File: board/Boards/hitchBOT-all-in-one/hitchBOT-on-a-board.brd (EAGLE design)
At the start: 100 x 55 mm, 16 parts

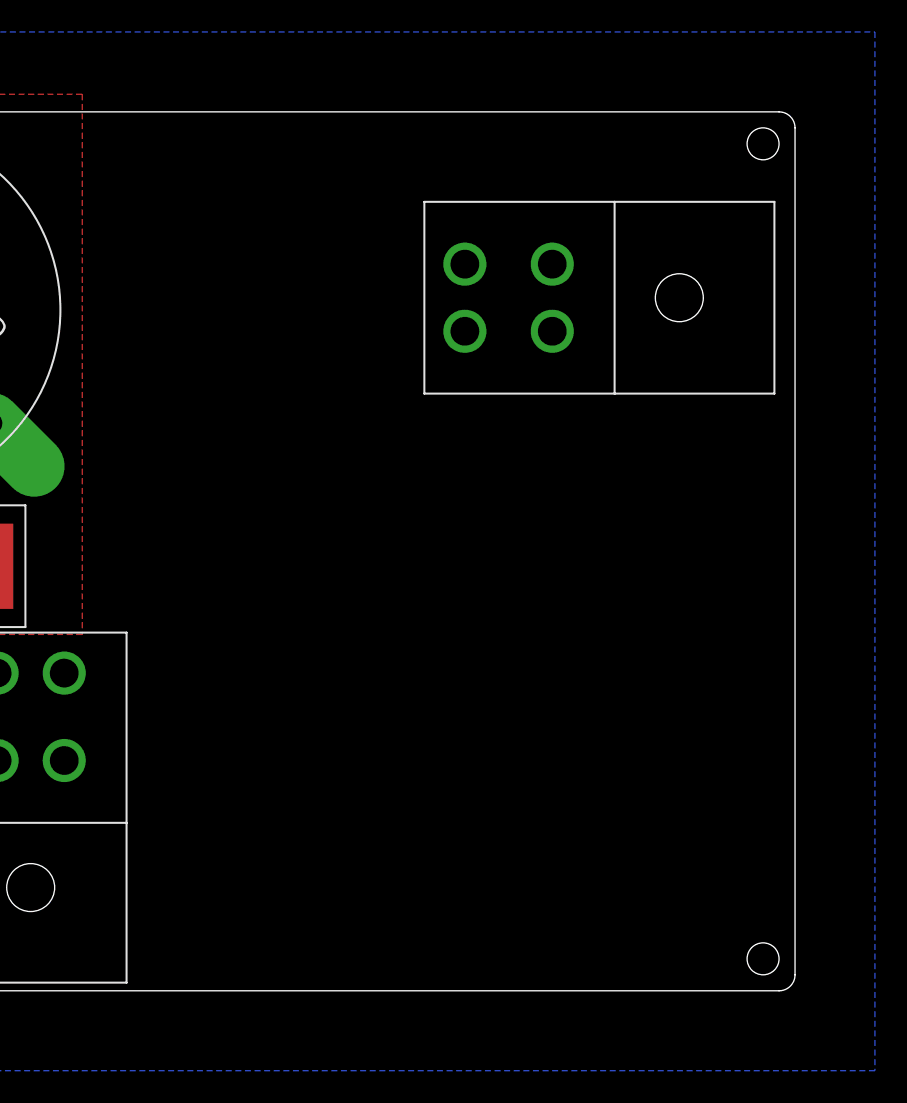
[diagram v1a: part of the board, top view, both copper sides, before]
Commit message: added microcontroller + started 5v switching circuit
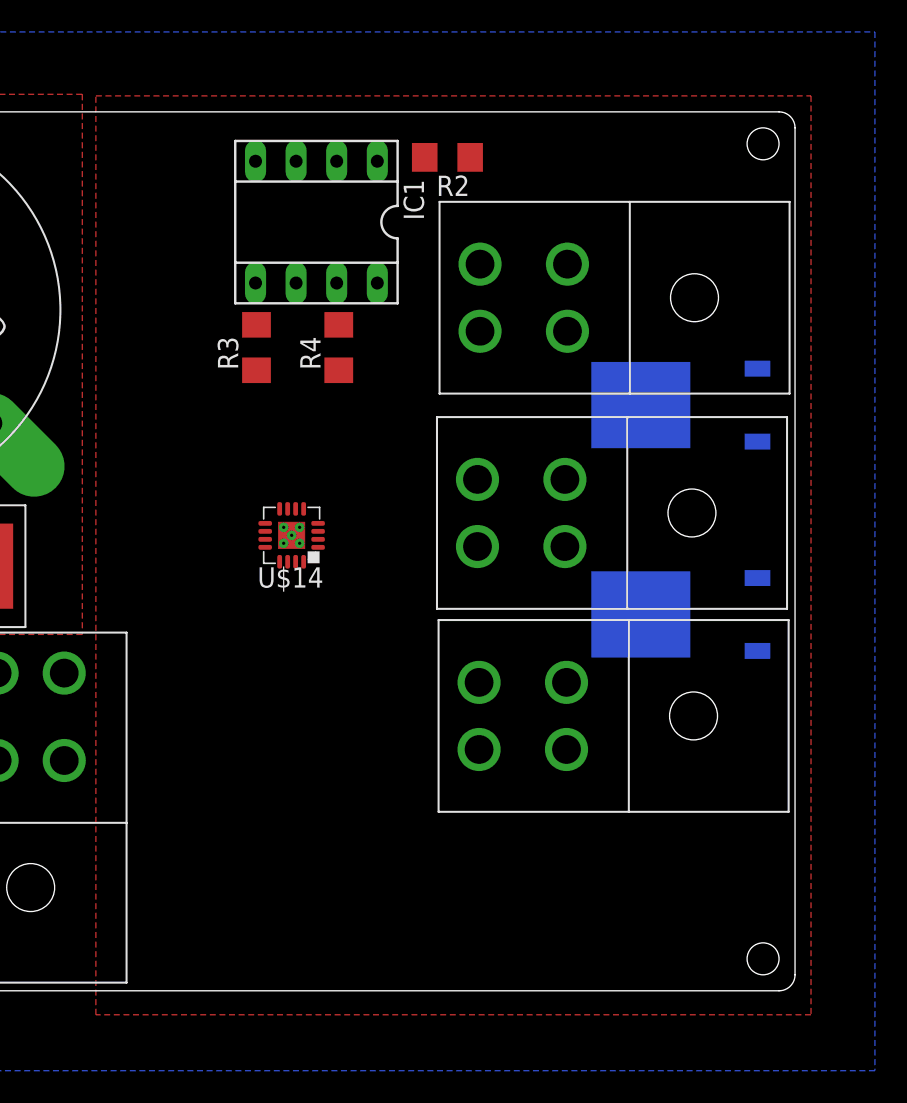
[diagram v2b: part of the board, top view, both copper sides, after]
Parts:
- added IC1: (no value), ic-package:SOCKET-08
- added Q1, Q2: SPD30P06PTO252, transistor-fet:TO252
- added R2, R3, R4: (no value), resistor:R1206
- added U$12, U$13: 2X2-MOLEX, Molex:2X2MOLEX
- added U$14: TPS62133, macgrid:QFN16
- moved U$11 0.95 mm to (83.7, 43.4)
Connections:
- new net N$10: Q2.3, U$12.GNDL, U$12.GNDR
- new net N$11: IC1.7, Q2.1, R4.2
- new net N$12: U$14.10, U$14.11, U$14.12, U$14.13
- new net N$13: IC1.5, Q1.1, R3.2
- new net N$7: IC1.1, R2.2
- new net N$8: R2.1, U$11.POWERL, U$11.POWERR, U$12.POWERL, U$12.POWERR, U$13.POWERL, U$13.POWERR
- new net N$9: Q1.3, U$13.GNDL, U$13.GNDR
- net GND: now also IC1.4, Q1.2, Q2.2, U$14.15, U$14.16, U$14.5, U$14.6, U$14.7, U$14.8, U$14.P$1
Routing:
- added copper zone on layer 1, net N$8
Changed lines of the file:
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@@
 <setting verticaltext="up"/>
 </settings>
-<grid distance="0.1" unitdist="mm" unit="mm" style="lines" multiple="1" display="no" altdistance="0.5" altunitdist="mm" altunit="mm"/>
+<grid distance="0.25" unitdist="mm" unit="mm" style="lines" multiple="1" display="no" altdistance="0.5" altunitdist="mm" altunit="mm"/>
 <layers>
 <layer number="1" name="Top" color="4" fill="1" visible="yes" active="yes"/>
@@
 <element name="U$9" library="macgrid" package="DO-214AB" value="DO-214AB" x="36.14" y="26.63"/>
 <element name="U$10" library="Molex" package="2X2MOLEX" value="2X2-MOLEX" x="16.51" y="34.96" rot="R270"/>
-<element name="U$11" library="Molex" package="2X2MOLEX" value="2X2-MOLEX" x="82.71" y="43.37" rot="R90"/>
+<element name="U$11" library="Molex" package="2X2MOLEX" value="2X2-MOLEX" x="83.66" y="43.37" rot="R90"/>
+<element name="Q1" library="transistor-fet" package="TO252" value="SPD30P06PTO252" x="92.85" y="23.55" smashed="yes" rot="MR270">
+<attribute name="NAME" x="95.39" y="27.36" size="1.27" layer="26" rot="MR0"/>
+</element>
+<element name="Q2" library="transistor-fet" package="TO252" value="SPD30P06PTO252" x="92.85" y="36.65" smashed="yes" rot="MR270">
+<attribute name="NAME" x="95.39" y="40.46" size="1.27" layer="26" rot="MR0"/>
+</element>
+<element name="IC1" library="ic-package" package="SOCKET-08" value="" x="70.05" y="48.1" rot="R180"/>
+<element name="R2" library="resistor" package="R1206" value="" x="78.25" y="52.15" rot="R180"/>
+<element name="R3" library="resistor" package="R1206" value="" x="66.3" y="40.25" rot="R90"/>
+<element name="R4" library="resistor" package="R1206" value="" x="71.45" y="40.25" rot="R90"/>
+<element name="U$12" library="Molex" package="2X2MOLEX" value="2X2-MOLEX" x="83.5" y="29.9" rot="R90"/>
+<element name="U$13" library="Molex" package="2X2MOLEX" value="2X2-MOLEX" x="83.6" y="17.2" rot="R90"/>
+<element name="U$14" library="macgrid" package="QFN16" value="TPS62133" x="68.5" y="28.5" rot="R180"/>
 </elements>
 <signals>
@@
 <contactref element="U$11" pad="GNDL"/>
 <contactref element="U$11" pad="GNDR"/>
-<wire x1="14.41" y1="37.06" x2="23.9" y2="43.79" width="0" layer="19" extent="1-1"/>
+<contactref element="IC1" pad="4"/>
+<contactref element="Q1" pad="2"/>
+<contactref element="Q2" pad="2"/>
+<contactref element="U$14" pad="5"/>
+<contactref element="U$14" pad="6"/>
+<contactref element="U$14" pad="16"/>
+<contactref element="U$14" pad="P$1"/>
+<contactref element="U$14" pad="15"/>
+<contactref element="U$14" pad="7"/>
+<contactref element="U$14" pad="8"/>
+<via x="68.5" y="28.5" extent="1-16" drill="0.2" diameter="0.254"/>
+<via x="68" y="29" extent="1-16" drill="0.2" diameter="0.254"/>
+<via x="69" y="29" extent="1-16" drill="0.2" diameter="0.254"/>
+<via x="68" y="28" extent="1-16" drill="0.2" diameter="0.254"/>
+<via x="69" y="28" extent="1-16" drill="0.2" diameter="0.254"/>
+<wire x1="68.75" y1="30.155" x2="69.25" y2="30.155" width="0" layer="19" extent="1-1"/>
+<wire x1="68.25" y1="30.155" x2="68.75" y2="30.155" width="0" layer="19" extent="1-1"/>
+<wire x1="67.75" y1="30.155" x2="68.25" y2="30.155" width="0" layer="19" extent="1-1"/>
+<wire x1="69" y1="29" x2="69.25" y2="30.155" width="0" layer="19" extent="1-1"/>
+<wire x1="69.25" y1="26.845" x2="69" y2="28" width="0" layer="19" extent="1-1"/>
+<wire x1="68.75" y1="26.845" x2="69.25" y2="26.845" width="0" layer="19" extent="1-1"/>
 <wire x1="10.43" y1="43.79" x2="14.41" y2="37.06" width="0" layer="19" extent="1-1"/>
 <wire x1="15.68" y1="14.73" x2="24.67" y2="14.41" width="0" layer="19" extent="1-1"/>
@@
 <wire x1="6.81" y1="19.47" x2="15.64" y2="19.47" width="0" layer="19" extent="1-1"/>
 <wire x1="6.87" y1="14.73" x2="6.81" y2="19.47" width="0" layer="19" extent="1-1"/>
+<wire x1="23.9" y1="43.79" x2="14.41" y2="37.06" width="0" layer="19" extent="1-1"/>
 </signal>
 <signal name="N$2">
@@
 </polygon>
 </signal>
+<signal name="N$7">
+<contactref element="R2" pad="2"/>
+<contactref element="IC1" pad="1"/>
+<wire x1="73.86" y1="51.91" x2="76.828" y2="52.15" width="0" layer="19" extent="1-1"/>
+</signal>
+<signal name="N$8">
+<contactref element="U$11" pad="POWERL"/>
+<contactref element="U$11" pad="POWERR"/>
+<contactref element="R2" pad="1"/>
+<contactref element="U$12" pad="POWERL"/>
+<contactref element="U$12" pad="POWERR"/>
+<contactref element="U$13" pad="POWERL"/>
+<contactref element="U$13" pad="POWERR"/>
+<polygon width="0.4064" layer="1">
+<vertex x="56.25" y="56"/>
+<vertex x="101" y="56"/>
+<vertex x="101" y="-1.5"/>
+<vertex x="56.25" y="-1.5"/>
+</polygon>
+</signal>
+<signal name="N$9">
+<contactref element="Q1" pad="3"/>
+<contactref element="U$13" pad="GNDL"/>
+<contactref element="U$13" pad="GNDR"/>
+<wire x1="85.7" y1="19.3" x2="90.35" y2="23.55" width="0" layer="19" extent="16-16"/>
+<wire x1="85.7" y1="15.1" x2="85.7" y2="19.3" width="0" layer="19" extent="1-1"/>
+</signal>
+<signal name="N$10">
+<contactref element="Q2" pad="3"/>
+<contactref element="U$12" pad="GNDL"/>
+<contactref element="U$12" pad="GNDR"/>
+<wire x1="85.6" y1="32" x2="90.35" y2="36.65" width="0" layer="19" extent="16-16"/>
+<wire x1="85.6" y1="27.8" x2="85.6" y2="32" width="0" layer="19" extent="1-1"/>
+</signal>
+<signal name="N$11">
+<contactref element="Q2" pad="1"/>
+<contactref element="R4" pad="2"/>
+<contactref element="IC1" pad="7"/>
+<wire x1="71.45" y1="41.672" x2="97.65" y2="38.93" width="0" layer="19" extent="1-16"/>
+<wire x1="71.32" y1="44.29" x2="71.45" y2="41.672" width="0" layer="19" extent="1-1"/>
+</signal>
+<signal name="N$13">
+<contactref element="IC1" pad="5"/>
+<contactref element="Q1" pad="1"/>
+<contactref element="R3" pad="2"/>
+<wire x1="66.3" y1="41.672" x2="97.65" y2="25.83" width="0" layer="19" extent="1-16"/>
+<wire x1="66.24" y1="44.29" x2="66.3" y2="41.672" width="0" layer="19" extent="1-1"/>
+</signal>
+<signal name="N$12">
+<contactref element="U$14" pad="12"/>
+<contactref element="U$14" pad="11"/>
+<contactref element="U$14" pad="10"/>
+<contactref element="U$14" pad="13"/>
+<wire x1="66.845" y1="28.75" x2="66.845" y2="28.25" width="0" layer="19" extent="1-1"/>
+<wire x1="66.845" y1="27.75" x2="66.845" y2="28.25" width="0" layer="19" extent="1-1"/>
+<wire x1="67.75" y1="26.845" x2="66.845" y2="27.75" width="0" layer="19" extent="1-1"/>
+</signal>
 </signals>

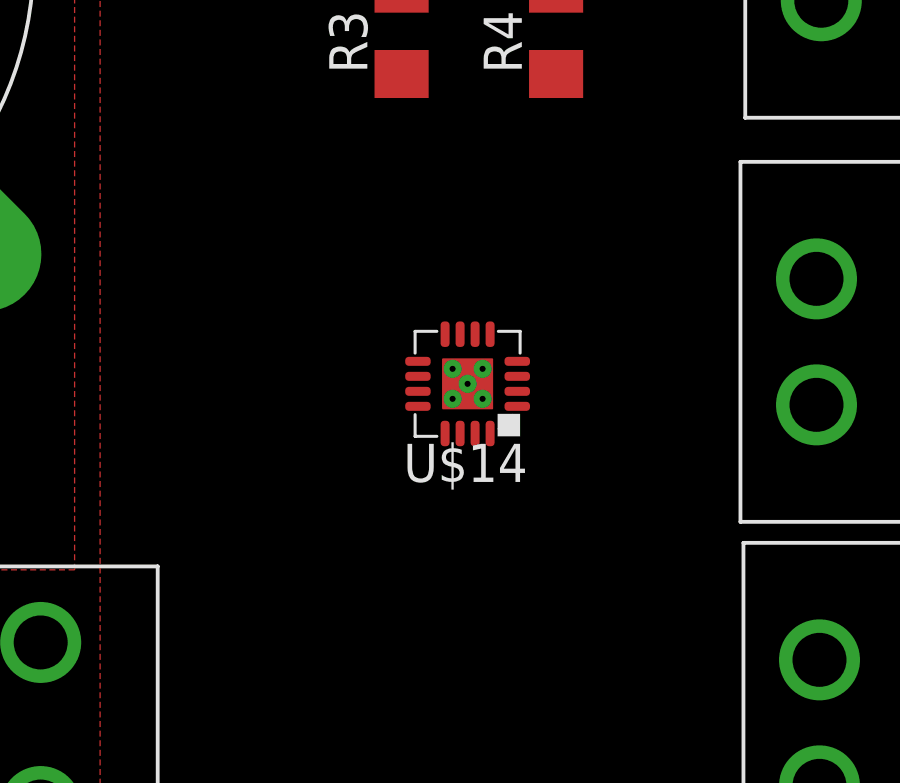
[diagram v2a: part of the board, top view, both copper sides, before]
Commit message: finished initial rough copy of the board, need to add LEDs and writing
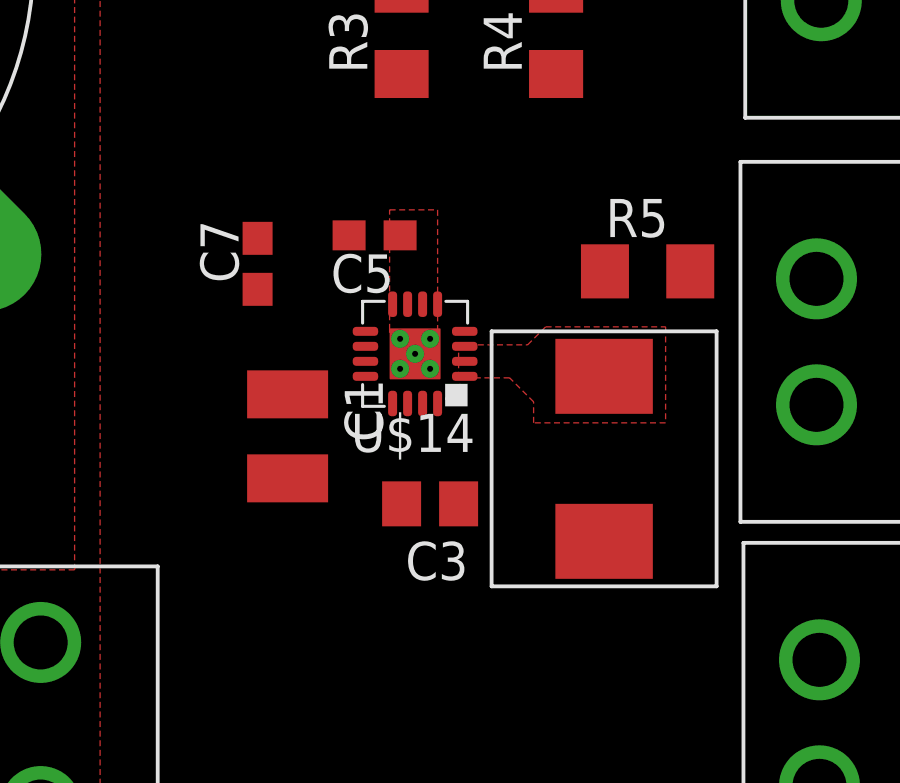
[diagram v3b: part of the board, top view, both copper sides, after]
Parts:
- added C11, C13: SMD-CAP-NICHICON-8MM, macgrid:SMD-CAP-8MM
- added C5: 3300pF, rcl:C0603
- added C7: 0.1uF, rcl:C0603
- added R5: 100k, resistor:R1206
- added U$15: DR73-2R2-R, macgrid:DR73-2R2-R
- C1: value SMD-CAP-NICHICON-8MM -> 10uF; device macgrid:SMD-CAP-8MM -> eagle-ltspice:C1210
- C3: value SMD-CAP-NICHICON-8MM -> 22uF; device macgrid:SMD-CAP-8MM -> rcl:C0805
- moved C1 55.8 mm to (62.5, 26.8), turned to 270 degrees
- moved C3 51.6 mm to (67.2, 24.5), turned to 180 degrees
- moved U$14 2.02 mm to (66.8, 29.5)
- renumbered C2 to C12, C4 to C14
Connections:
- removed net N$12: U$14.10, U$14.11, U$14.12, U$14.13
- new net N$14: U$14.1, U$14.2, U$14.3, U$15.P$1
- new net N$15: C3.1, IC1.8, R2.1, R3.1, R4.1, R5.1, U$14.14, U$15.P$2
- new net N$16: R5.2, U$14.4
- new net N$17: C5.2, U$14.9
- net GND: now also C1.2, C11.P-, C13.P-, C3.2, C5.1, C7.2; no longer C1.P-, C3.P-
- net N$1: now also C11.P+, C13.P+; no longer C1.P+, C3.P+
- net N$8: now also C1.1, C7.1, U$14.10, U$14.11, U$14.12, U$14.13; no longer R2.1
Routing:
- added copper zone on layer 1, net GND
- added copper zone on layer 1, net N$14

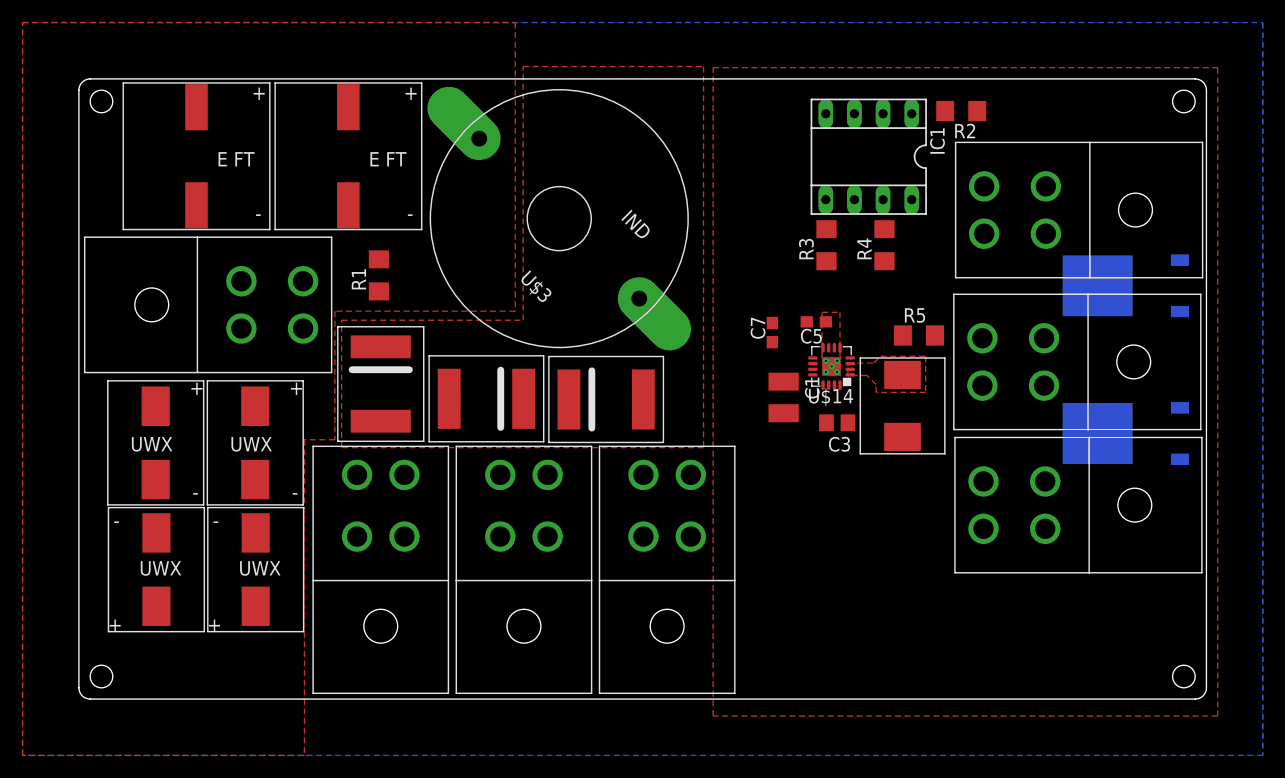
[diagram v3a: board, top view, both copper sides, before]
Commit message: added status LED and molex power adapters for all three voltage areas
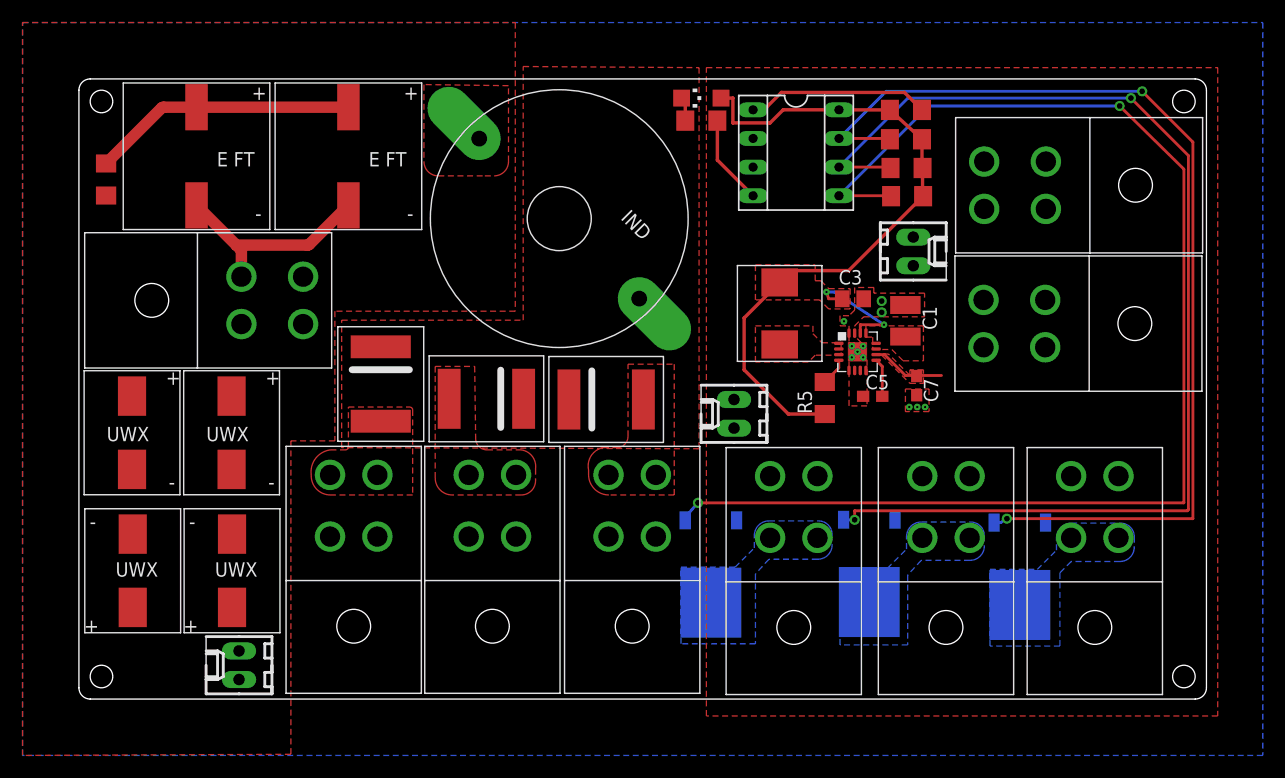
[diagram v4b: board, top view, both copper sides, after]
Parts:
- added J1, J2, J3: 22-27-2021-02, con-molex:6410-02
- added LED1: (no value), led:CHIPLED_1206
- added Q3: SPD30P06PTO252, transistor-fet:TO252
- added R6: (no value), resistor:R1206
- added R7: (no value), rcl:R1206
- added U$16, U$17: 2X2-MOLEX, Molex:2X2MOLEX
- moved Q1 38.9 mm to (56.0, 11.1), turned to 180 degrees
- moved Q2 27.5 mm to (83.5, 10.8), turned to 180 degrees
- moved R1 25.6 mm to (2.41, 46.1)
- moved U$13 20.2 mm to (63.4, 16.4), turned to 0 degrees
- moved U$12 15.0 mm to (90.1, 16.4), turned to 0 degrees
- moved U$15 13.6 mm to (62.1, 34.2), turned to 90 degrees
- moved C7 13.6 mm to (74.3, 27.8), turned to 270 degrees
- moved C1 12.8 mm to (73.3, 33.5), turned to 90 degrees
- moved C3 11.1 mm to (68.7, 35.5), turned to 0 degrees
- moved R5 10.0 mm to (66.2, 26.7), turned to 90 degrees
- moved R4 9.59 mm to (73.3, 49.6), turned to 180 degrees
- moved R3 8.37 mm to (73.5, 44.6), turned to 180 degrees
- moved C5 8.28 mm to (70.4, 26.9), turned to 0 degrees
- moved IC1 6.46 mm to (63.6, 48.5), turned to 270 degrees
- moved R2 4.90 mm to (73.3, 52.2), turned to 0 degrees
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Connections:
- new net N$18: Q3.3, U$17.GNDL, U$17.GNDR
- new net N$19: IC1.6, Q3.1, R6.2
- new net N$20: LED1.C, R7.2
- net GND: now also J1.1, J2.1, J3.1, Q3.2, R7.1, U$16.GNDL, U$16.GNDR
- net N$1: now also J2.2
- net N$15: now also J1.2, LED1.A, R6.1
- net N$8: now also J3.2, U$16.POWERL, U$16.POWERR, U$17.POWERL, U$17.POWERR
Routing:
- net N$13: track 0.00 -> 115.4 mm, vias 0 -> 2
- net N$19: track 0.00 -> 103.1 mm, vias 0 -> 2
- net N$11: track 0.00 -> 90.7 mm, vias 0 -> 2
- net N$15: track 0.00 -> 71.1 mm, vias 0 -> 2
- net GND: track 0.00 -> 27.3 mm, vias 5 -> 11
- net N$2: track 0.00 -> 23.5 mm
- net N$7: track 0.00 -> 16.3 mm
- net N$8: track 0.00 -> 6.63 mm
- net N$17: track 0.00 -> 3.43 mm
- net N$16: track 0.00 -> 2.44 mm
- net N$20: track 0.00 -> 2.33 mm
- added copper zone on layer 16, net N$10
- added copper zone on layer 1, net N$12
- added copper zone on layer 1, net N$15
- added copper zone on layer 16, net N$18
- added copper zone on layer 1, net N$3
- added copper zone on layer 1, net N$4
- added copper zone on layer 1, net N$5
- added copper zone on layer 16, net N$9
